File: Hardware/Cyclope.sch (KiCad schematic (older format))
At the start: 10 parts, among them M1 FS5113R, M2 FS5113R

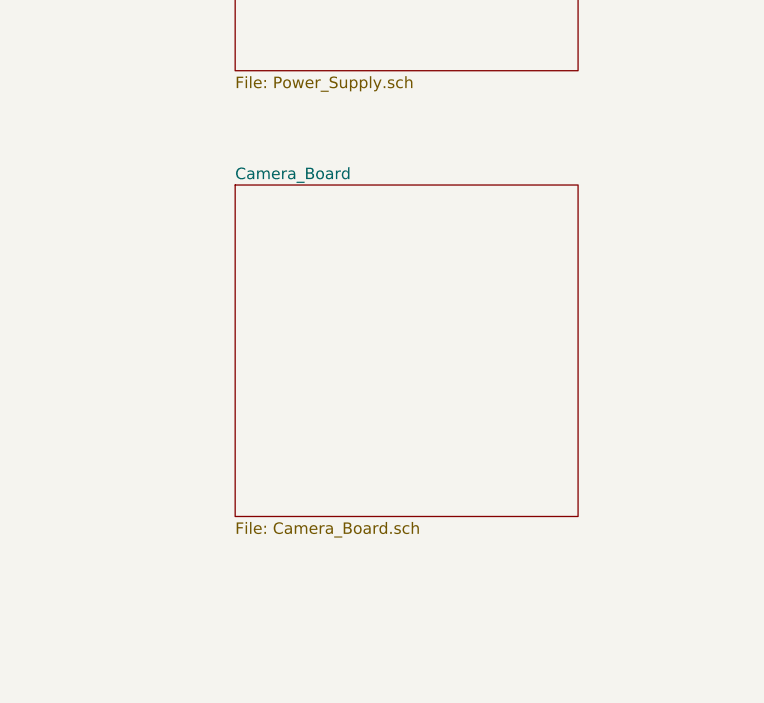
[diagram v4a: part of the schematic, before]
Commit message: [Hardware] Renamed 'camera board' to 'front board' as this board is not only carrying the camera.
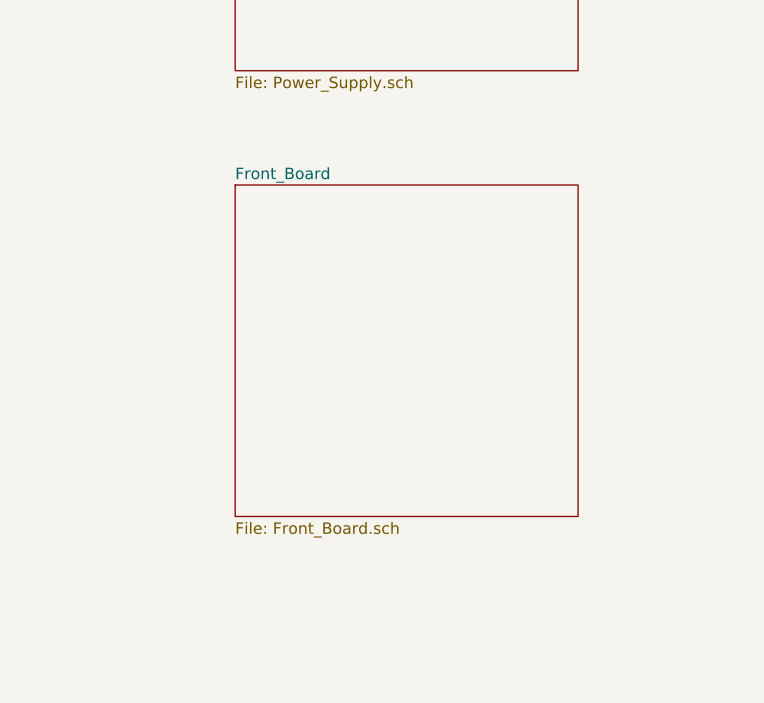
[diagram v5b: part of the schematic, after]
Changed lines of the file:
@@
 S 2500 4000 1500 1450
 U 5F288D93
-F0 "Camera_Board" 50
-F1 "Camera_Board.sch" 50
+F0 "Front_Board" 50
+F1 "Front_Board.sch" 50
 $EndSheet
 $Comp

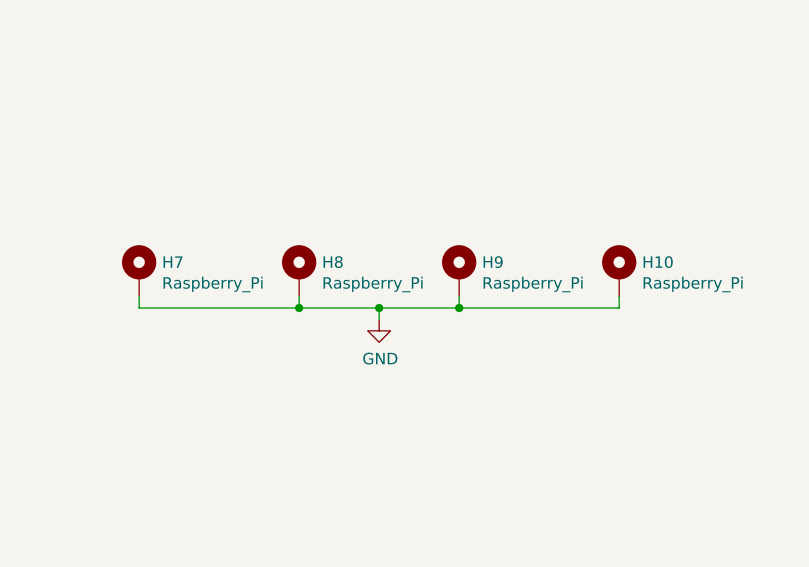
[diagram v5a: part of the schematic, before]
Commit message: (Hardware] Renamed motherboard PCB mounting holes for more coherency.
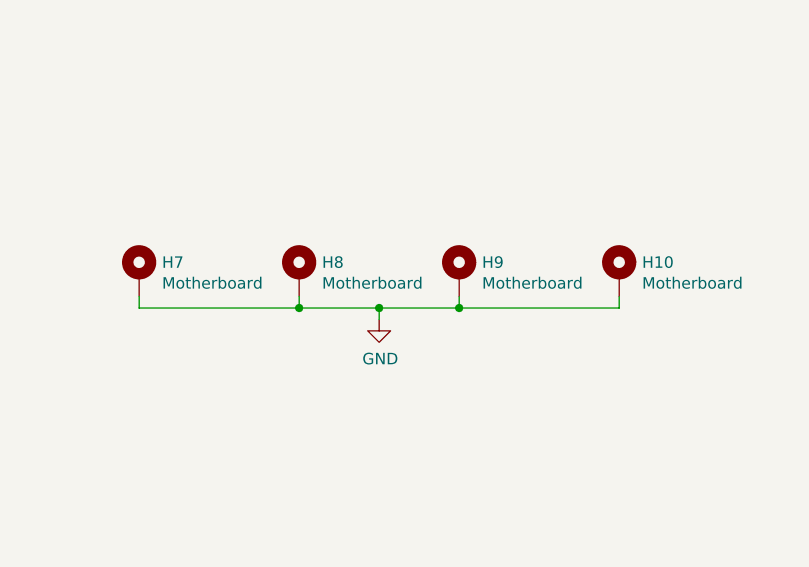
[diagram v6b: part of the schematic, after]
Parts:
- H10, H7, H8, H9: value Raspberry_Pi -> Motherboard
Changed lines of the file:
@@
 P 6150 5050
 F 0 "H7" H 6250 5099 50  0000 L CNN
-F 1 "Raspberry_Pi" H 6250 5008 50  0000 L CNN
+F 1 "Motherboard" H 6250 5008 50  0000 L CNN
 F 2 "MountingHole:MountingHole_3.2mm_M3_Pad" H 6150 5050 50  0001 C CNN
 F 3 "~" H 6150 5050 50  0001 C CNN
@@
 P 6850 5050
 F 0 "H8" H 6950 5099 50  0000 L CNN
-F 1 "Raspberry_Pi" H 6950 5008 50  0000 L CNN
+F 1 "Motherboard" H 6950 5008 50  0000 L CNN
 F 2 "MountingHole:MountingHole_3.2mm_M3_Pad" H 6850 5050 50  0001 C CNN
 F 3 "~" H 6850 5050 50  0001 C CNN
@@
 P 7550 5050
 F 0 "H9" H 7650 5099 50  0000 L CNN
-F 1 "Raspberry_Pi" H 7650 5008 50  0000 L CNN
+F 1 "Motherboard" H 7650 5008 50  0000 L CNN
 F 2 "MountingHole:MountingHole_3.2mm_M3_Pad" H 7550 5050 50  0001 C CNN
 F 3 "~" H 7550 5050 50  0001 C CNN
@@
 P 8250 5050
 F 0 "H10" H 8350 5099 50  0000 L CNN
-F 1 "Raspberry_Pi" H 8350 5008 50  0000 L CNN
+F 1 "Motherboard" H 8350 5008 50  0000 L CNN
 F 2 "MountingHole:MountingHole_3.2mm_M3_Pad" H 8250 5050 50  0001 C CNN
 F 3 "~" H 8250 5050 50  0001 C CNN

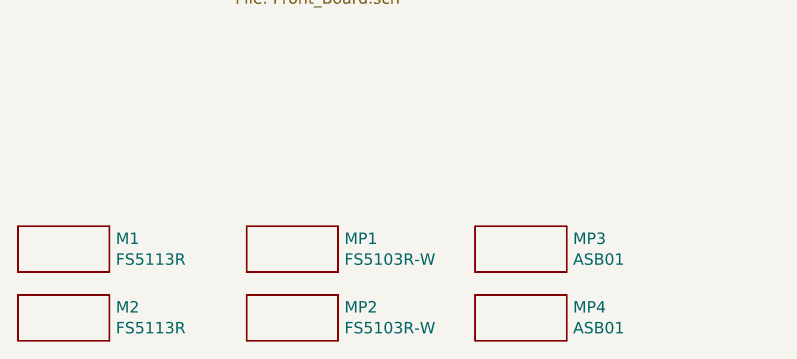
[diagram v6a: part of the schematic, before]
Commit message: [Hardware] Removed mechanical supply parts unrelated with PCB, added battery holder supply part.
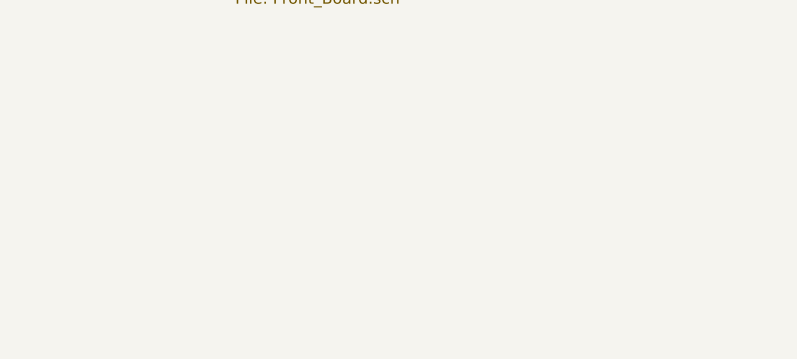
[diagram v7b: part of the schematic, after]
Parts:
- removed M1, M2: FS5113R, Supply_Part:Supply_Part, symbol Supply_Part:Supply_Part
- removed MP1, MP2: FS5103R-W, Supply_Part:Supply_Part, symbol Supply_Part:Supply_Part
- removed MP3, MP4: ASB01, Supply_Part:Supply_Part, symbol Supply_Part:Supply_Part
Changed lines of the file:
@@
 F1 "ADC.sch" 50
 $EndSheet
-$Comp
-L Supply_Part:Supply_Part M?
-U 1 1 5F27E4DF
-P 1750 6900
-AR Path="/5F22814A/5F27E4DF" Ref="M?"  Part="1"
-AR Path="/5F27E4DF" Ref="M2"  Part="1"
-F 0 "M2" H 1978 6946 50  0000 L CNN
-F 1 "FS5113R" H 1978 6855 50  0000 L CNN
-F 2 "Supply_Part:Supply_Part" H 1750 6900 50  0001 C CNN
-F 3 "" H 1750 6900 50  0001 C CNN
-F 4 "Manufacturer" H 1750 6900 50  0001 C CNN "Value2"
-	1    1750 6900
-	1    0    0    -1
-$EndComp
-$Comp
-L Supply_Part:Supply_Part M?
-U 1 1 5F28128C
-P 1750 6600
-AR Path="/5F22814A/5F28128C" Ref="M?"  Part="1"
-AR Path="/5F28128C" Ref="M1"  Part="1"
-F 0 "M1" H 1978 6646 50  0000 L CNN
-F 1 "FS5113R" H 1978 6555 50  0000 L CNN
-F 2 "Supply_Part:Supply_Part" H 1750 6600 50  0001 C CNN
-F 3 "" H 1750 6600 50  0001 C CNN
-F 4 "Feetech" H 1750 6600 50  0001 C CNN "Manufacturer"
-	1    1750 6600
-	1    0    0    -1
-$EndComp
-$Comp
-L Supply_Part:Supply_Part M?
-U 1 1 5F281D4B
-P 2750 6600
-AR Path="/5F22814A/5F281D4B" Ref="M?"  Part="1"
-AR Path="/5F281D4B" Ref="MP1"  Part="1"
-F 0 "MP1" H 2978 6646 50  0000 L CNN
-F 1 "FS5103R-W" H 2978 6555 50  0000 L CNN
-F 2 "Supply_Part:Supply_Part" H 2750 6600 50  0001 C CNN
-F 3 "" H 2750 6600 50  0001 C CNN
-F 4 "Feetech" H 2750 6600 50  0001 C CNN "Manufacturer"
-F 5 "Wheel" H 2750 6600 50  0001 C CNN "Value2"
-	1    2750 6600
-	1    0    0    -1
-$EndComp
-$Comp
-L Supply_Part:Supply_Part M?
-U 1 1 5F2828BE
-P 2750 6900
-AR Path="/5F22814A/5F2828BE" Ref="M?"  Part="1"
-AR Path="/5F2828BE" Ref="MP2"  Part="1"
-F 0 "MP2" H 2978 6946 50  0000 L CNN
-F 1 "FS5103R-W" H 2978 6855 50  0000 L CNN
-F 2 "Supply_Part:Supply_Part" H 2750 6900 50  0001 C CNN
-F 3 "" H 2750 6900 50  0001 C CNN
-F 4 "Feetech" H 2750 6900 50  0001 C CNN "Manufacturer"
-F 5 "Wheel" H 2750 6900 50  0001 C CNN "Value2"
-	1    2750 6900
-	1    0    0    -1
-$EndComp
-$Comp
-L Supply_Part:Supply_Part MP?
-U 1 1 5F283565
-P 3750 6600
-AR Path="/5F22814A/5F283565" Ref="MP?"  Part="1"
-AR Path="/5F283565" Ref="MP3"  Part="1"
-F 0 "MP3" H 3978 6646 50  0000 L CNN
-F 1 "ASB01" H 3978 6555 50  0000 L CNN
-F 2 "Supply_Part:Supply_Part" H 3750 6600 50  0001 C CNN
-F 3 "" H 3750 6600 50  0001 C CNN
-F 4 "Servomotor support" H 3750 6600 50  0001 C CNN "Value2"
-F 5 "https://www.gotronic.fr/art-support-de-servos-asb01-11637.htm" H 3750 6600 50  0001 C CNN "PurchaseLink"
-	1    3750 6600
-	1    0    0    -1
-$EndComp
-$Comp
-L Supply_Part:Supply_Part MP?
-U 1 1 5F283D48
-P 3750 6900
-AR Path="/5F22814A/5F283D48" Ref="MP?"  Part="1"
-AR Path="/5F283D48" Ref="MP4"  Part="1"
-F 0 "MP4" H 3978 6946 50  0000 L CNN
-F 1 "ASB01" H 3978 6855 50  0000 L CNN
-F 2 "Supply_Part:Supply_Part" H 3750 6900 50  0001 C CNN
-F 3 "" H 3750 6900 50  0001 C CNN
-F 4 "Servomotor support" H 3750 6900 50  0001 C CNN "Value2"
-F 5 "https://www.gotronic.fr/art-support-de-servos-asb01-11637.htm" H 3750 6900 50  0001 C CNN "PurchaseLink"
-	1    3750 6900
-	1    0    0    -1
-$EndComp
 $Sheet
 S 2500 4000 1500 1450

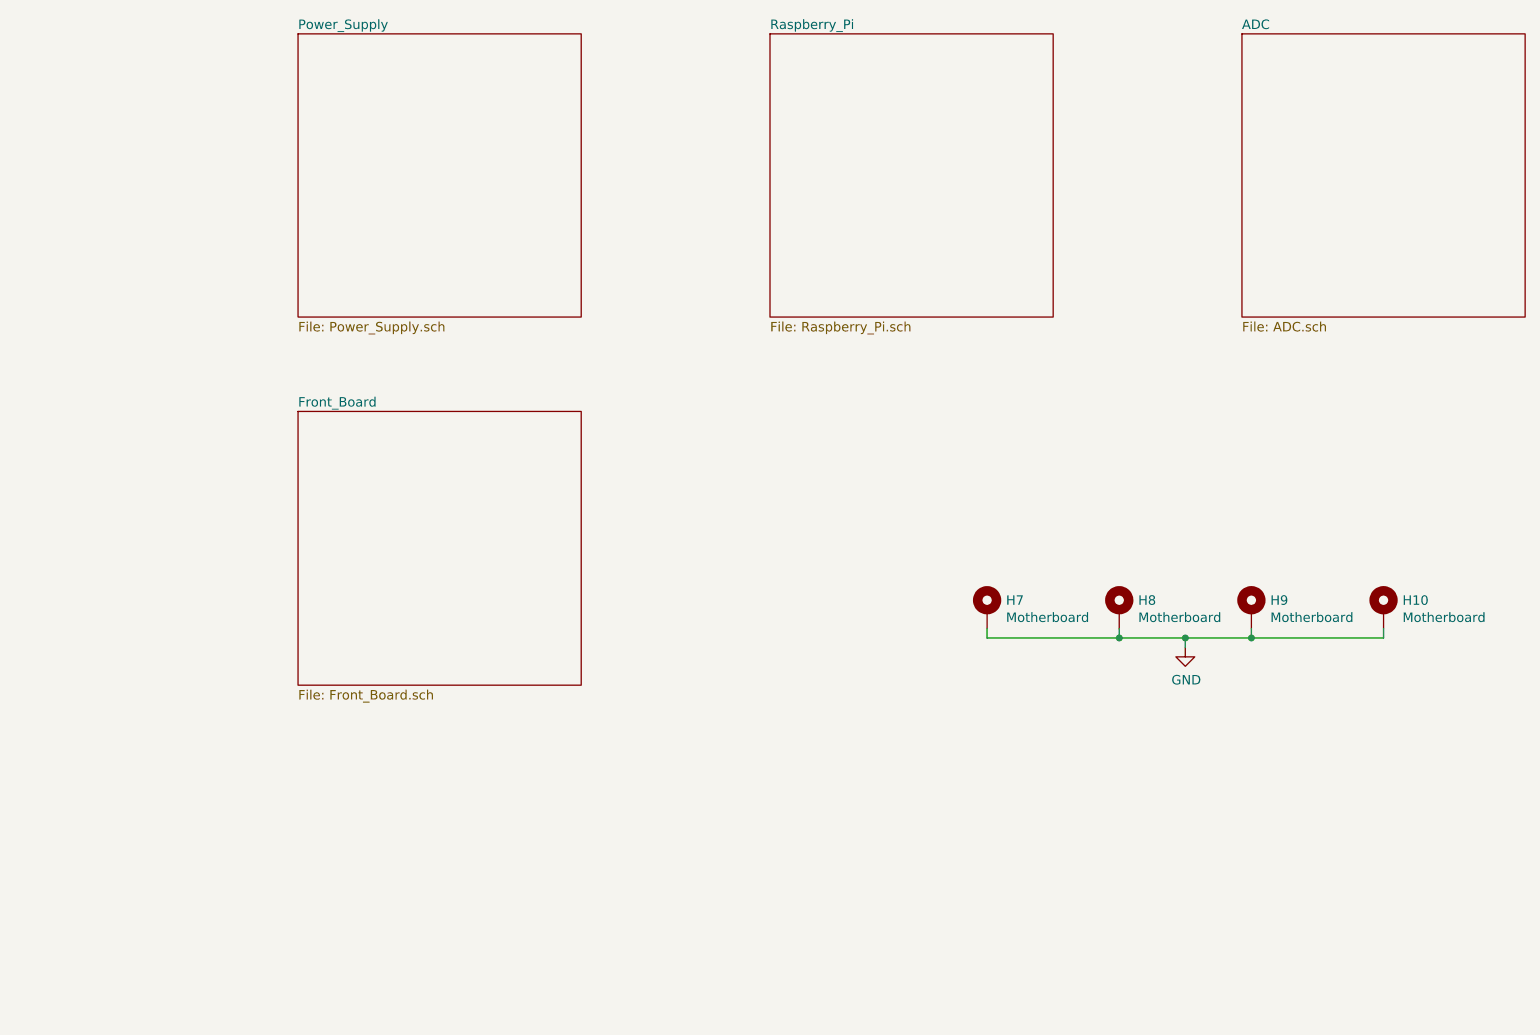
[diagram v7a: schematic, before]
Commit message: [Hardware] Added lidar support to schematic.
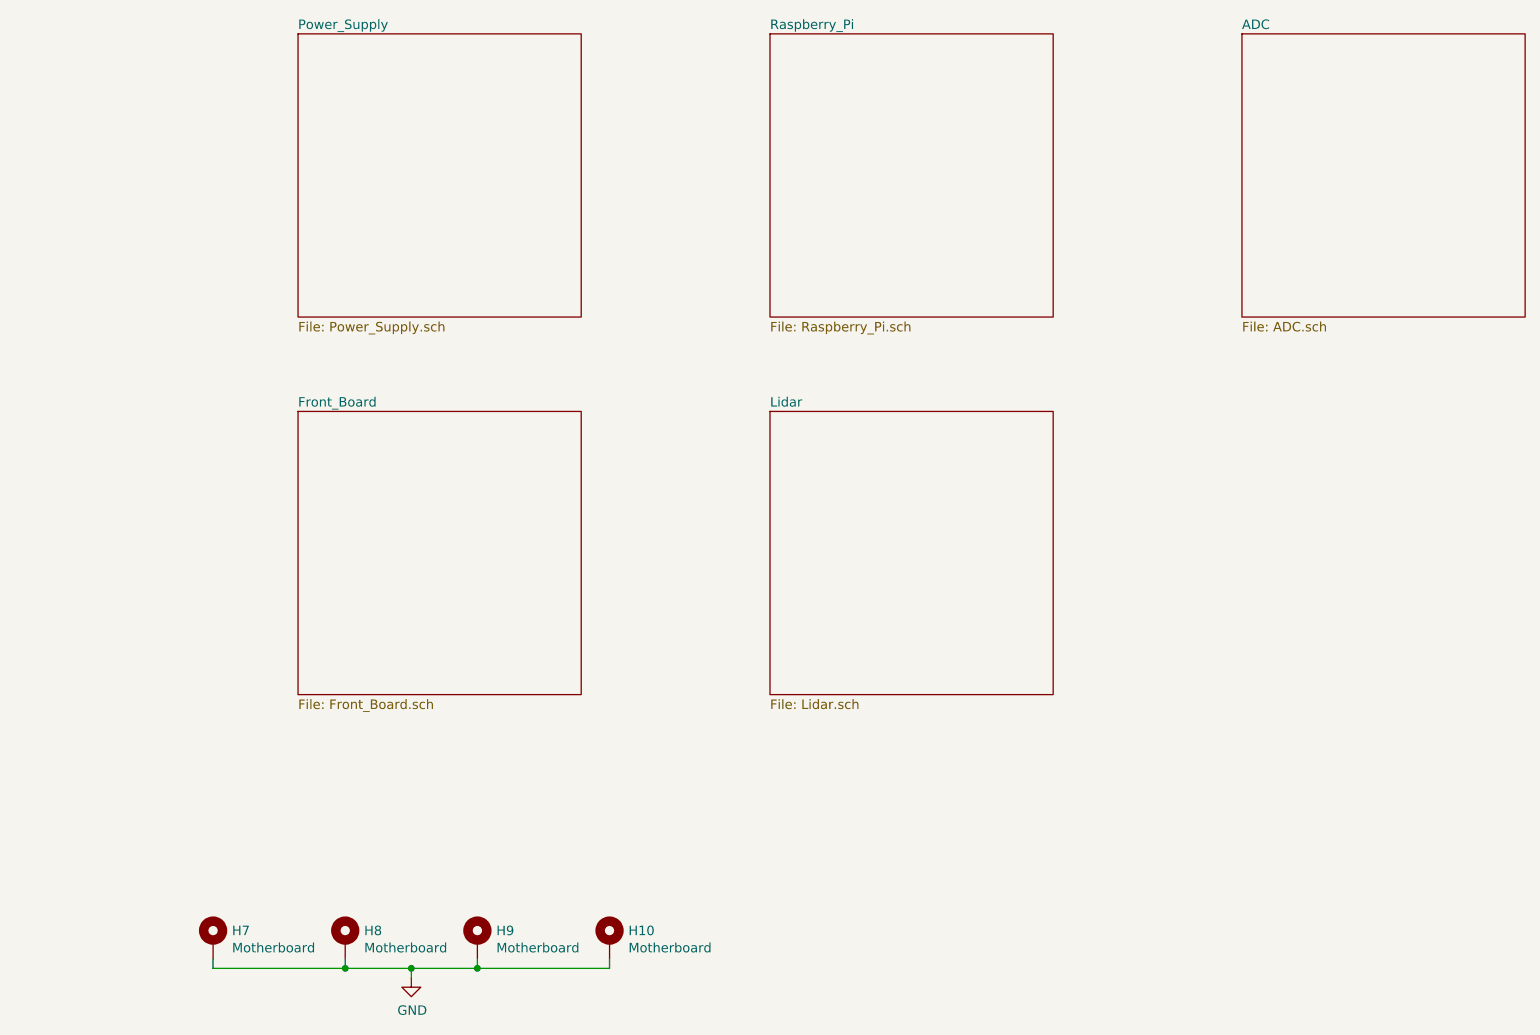
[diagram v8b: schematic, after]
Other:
- moved on the sheet: H10, H7, H8, H9
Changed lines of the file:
@@
 $Descr A4 11693 8268
 encoding utf-8
-Sheet 1 5
+Sheet 1 6
 Title "Main page"
-Date "2020-07-27"
-Rev "1.0"
+Date "2021-02-05"
+Rev "1.1"
 Comp "Cyclope robot by Adrien RICCIARDI"
 Comment1 ""
@@
 $EndSheet
 $Sheet
-S 2500 4000 1500 1450
+S 2500 4000 1500 1500
 U 5F288D93
 F0 "Front_Board" 50
@@
 L Mechanical:MountingHole_Pad H7
 U 1 1 5F3532F6
-P 6150 5050
-F 0 "H7" H 6250 5099 50  0000 L CNN
-F 1 "Motherboard" H 6250 5008 50  0000 L CNN
-F 2 "MountingHole:MountingHole_3.2mm_M3_Pad" H 6150 5050 50  0001 C CNN
-F 3 "~" H 6150 5050 50  0001 C CNN
-	1    6150 5050
+P 2050 6800
+F 0 "H7" H 2150 6849 50  0000 L CNN
+F 1 "Motherboard" H 2150 6758 50  0000 L CNN
+F 2 "MountingHole:MountingHole_3.2mm_M3_Pad" H 2050 6800 50  0001 C CNN
+F 3 "~" H 2050 6800 50  0001 C CNN
+	1    2050 6800
 	1    0    0    -1
 $EndComp
@@
 L Mechanical:MountingHole_Pad H8
 U 1 1 5F353CDE
-P 6850 5050
-F 0 "H8" H 6950 5099 50  0000 L CNN
-F 1 "Motherboard" H 6950 5008 50  0000 L CNN
-F 2 "MountingHole:MountingHole_3.2mm_M3_Pad" H 6850 5050 50  0001 C CNN
-F 3 "~" H 6850 5050 50  0001 C CNN
-	1    6850 5050
+P 2750 6800
+F 0 "H8" H 2850 6849 50  0000 L CNN
+F 1 "Motherboard" H 2850 6758 50  0000 L CNN
+F 2 "MountingHole:MountingHole_3.2mm_M3_Pad" H 2750 6800 50  0001 C CNN
+F 3 "~" H 2750 6800 50  0001 C CNN
+	1    2750 6800
 	1    0    0    -1
 $EndComp
@@
 L Mechanical:MountingHole_Pad H9
 U 1 1 5F35418A
-P 7550 5050
-F 0 "H9" H 7650 5099 50  0000 L CNN
-F 1 "Motherboard" H 7650 5008 50  0000 L CNN
-F 2 "MountingHole:MountingHole_3.2mm_M3_Pad" H 7550 5050 50  0001 C CNN
-F 3 "~" H 7550 5050 50  0001 C CNN
-	1    7550 5050
+P 3450 6800
+F 0 "H9" H 3550 6849 50  0000 L CNN
+F 1 "Motherboard" H 3550 6758 50  0000 L CNN
+F 2 "MountingHole:MountingHole_3.2mm_M3_Pad" H 3450 6800 50  0001 C CNN
+F 3 "~" H 3450 6800 50  0001 C CNN
+	1    3450 6800
 	1    0    0    -1
 $EndComp
@@
 L Mechanical:MountingHole_Pad H10
 U 1 1 5F3543C8
-P 8250 5050
-F 0 "H10" H 8350 5099 50  0000 L CNN
-F 1 "Motherboard" H 8350 5008 50  0000 L CNN
-F 2 "MountingHole:MountingHole_3.2mm_M3_Pad" H 8250 5050 50  0001 C CNN
-F 3 "~" H 8250 5050 50  0001 C CNN
-	1    8250 5050
+P 4150 6800
+F 0 "H10" H 4250 6849 50  0000 L CNN
+F 1 "Motherboard" H 4250 6758 50  0000 L CNN
+F 2 "MountingHole:MountingHole_3.2mm_M3_Pad" H 4150 6800 50  0001 C CNN
+F 3 "~" H 4150 6800 50  0001 C CNN
+	1    4150 6800
 	1    0    0    -1
 $EndComp
@@
 L power:GND #PWR018
 U 1 1 5F3568FB
-P 7200 5250
-F 0 "#PWR018" H 7200 5000 50  0001 C CNN
-F 1 "GND" H 7205 5077 50  0000 C CNN
-F 2 "" H 7200 5250 50  0001 C CNN
-F 3 "" H 7200 5250 50  0001 C CNN
-	1    7200 5250
+P 3100 7000
+F 0 "#PWR018" H 3100 6750 50  0001 C CNN
+F 1 "GND" H 3105 6827 50  0000 C CNN
+F 2 "" H 3100 7000 50  0001 C CNN
+F 3 "" H 3100 7000 50  0001 C CNN
+	1    3100 7000
 	1    0    0    -1
 $EndComp
 Wire Wire Line
-	6150 5150 6150 5200
+	2050 6900 2050 6950
 Wire Wire Line
-	6150 5200 6850 5200
+	2050 6950 2750 6950
 Wire Wire Line
-	6850 5200 6850 5150
+	2750 6950 2750 6900
 Wire Wire Line
-	6850 5200 7200 5200
+	2750 6950 3100 6950
 Wire Wire Line
-	7200 5200 7200 5250
-Connection ~ 6850 5200
+	3100 6950 3100 7000
+Connection ~ 2750 6950
 Wire Wire Line
-	7200 5200 7550 5200
-Connection ~ 7200 5200
+	3100 6950 3450 6950
+Connection ~ 3100 6950
 Wire Wire Line
-	7550 5200 7550 5150
-Connection ~ 7550 5200
+	3450 6950 3450 6900
+Connection ~ 3450 6950
 Wire Wire Line
-	8250 5200 8250 5150
+	4150 6950 4150 6900
 Wire Wire Line
-	7550 5200 8250 5200
+	3450 6950 4150 6950
+$Sheet
+S 5000 4000 1500 1500
+U 601E5913
+F0 "Lidar" 50
+F1 "Lidar.sch" 50
+$EndSheet
 $EndSCHEMATC
